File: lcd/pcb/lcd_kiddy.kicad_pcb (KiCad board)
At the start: 2 copper layers, 47 x 72 mm, 4 parts, among them J1 CONN_02X08, J3 BARREL_JACK, U1 ATMEGA168A-PU

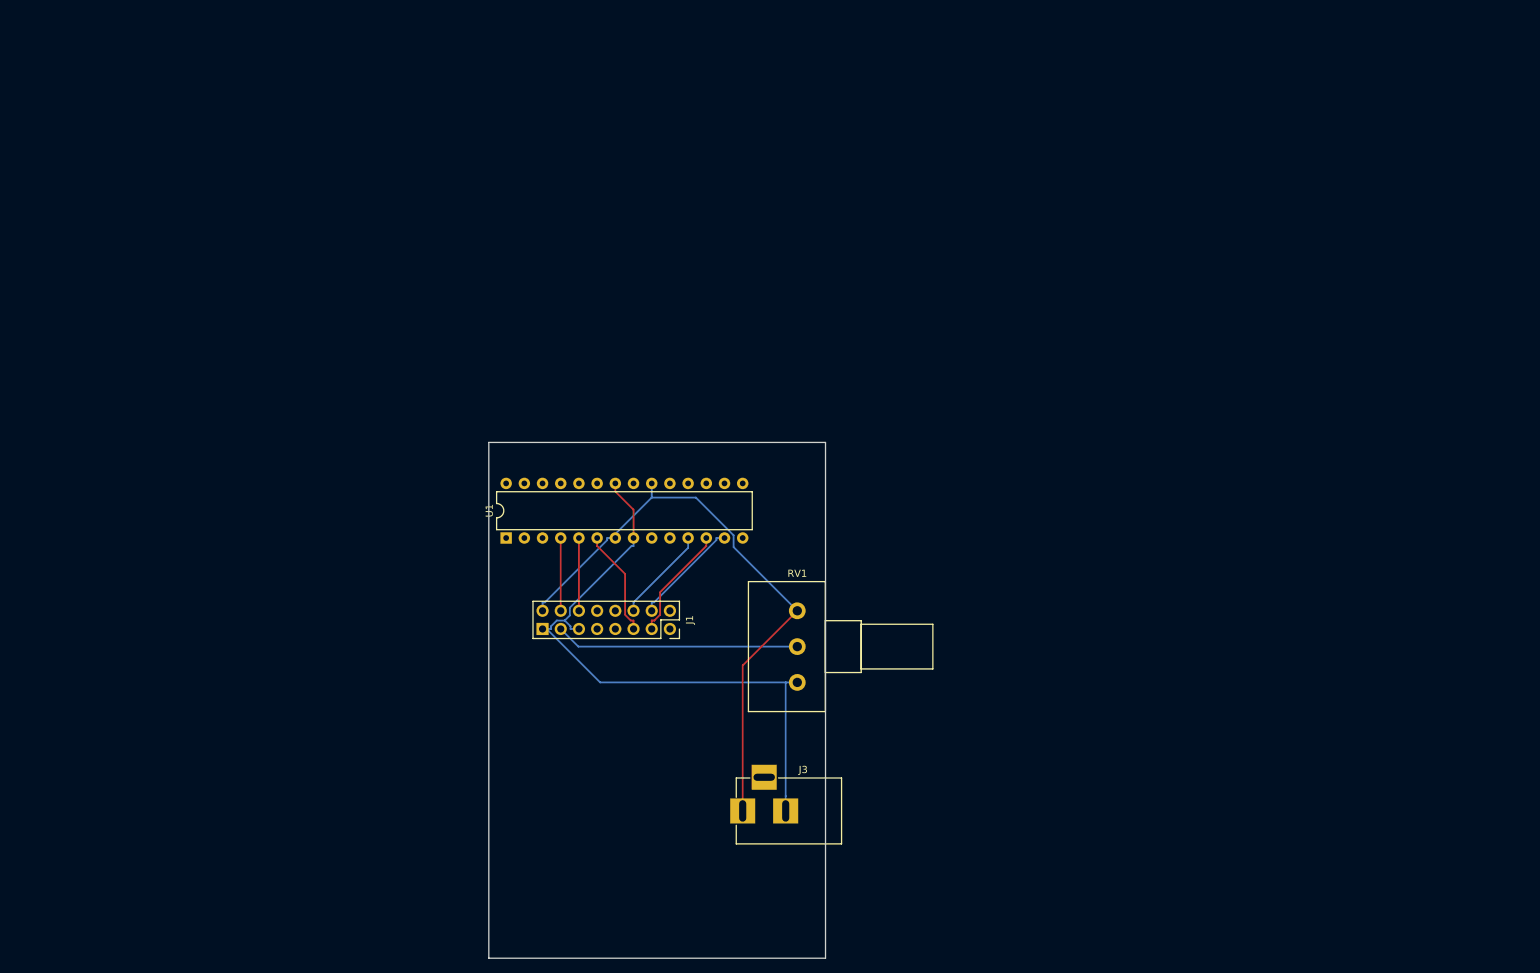
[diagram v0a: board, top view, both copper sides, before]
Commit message: LCDとatmega168aの配線方法を書いた。
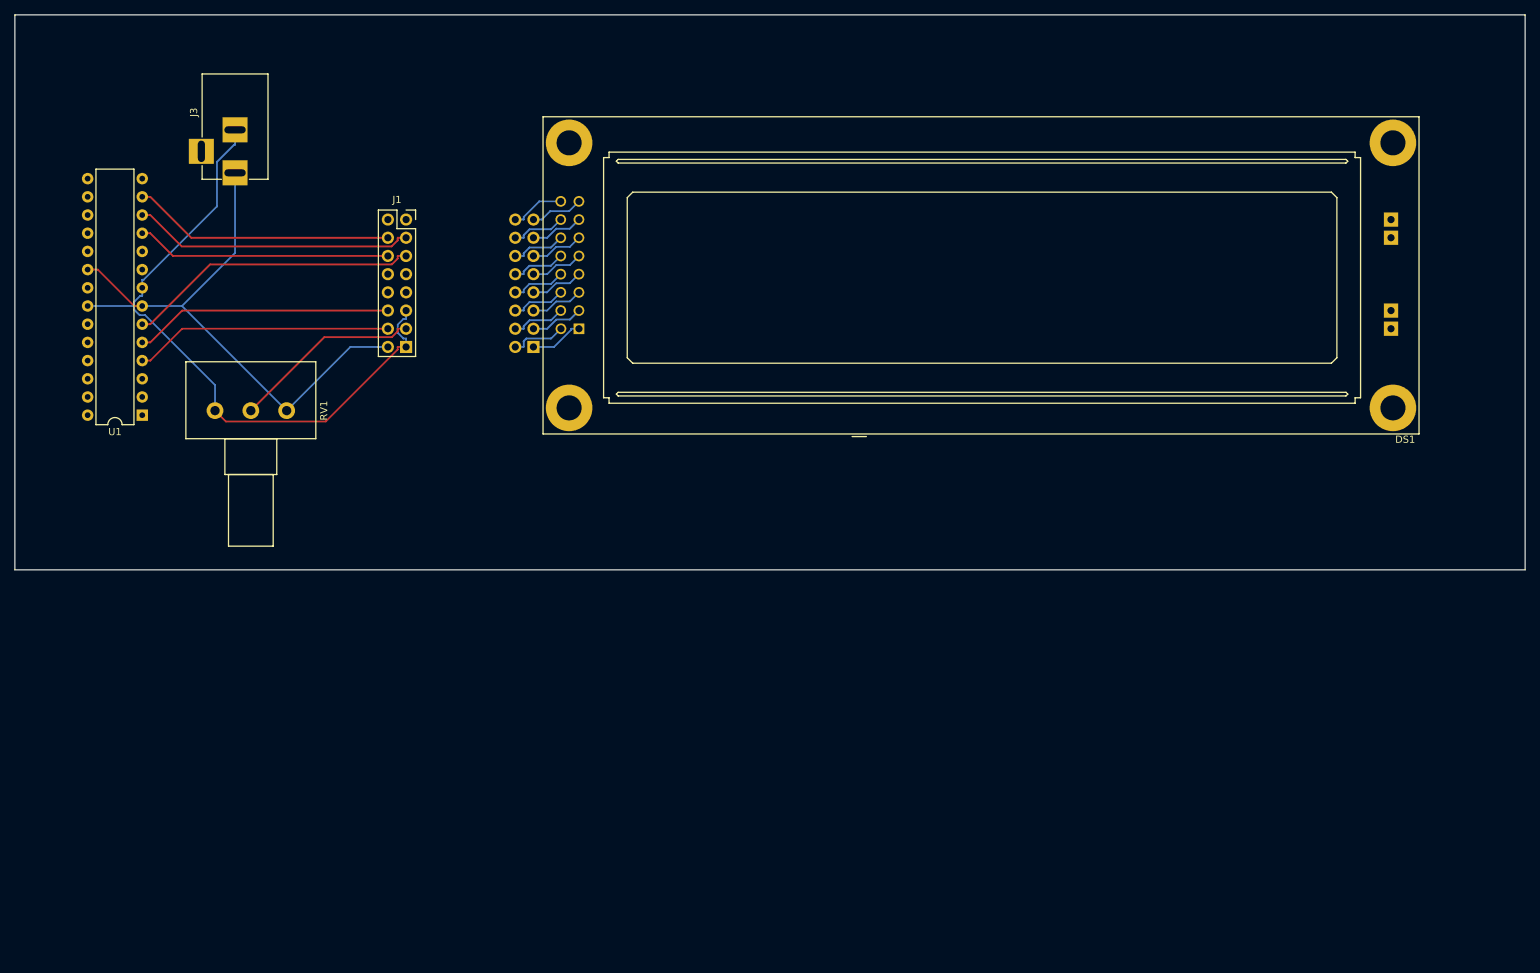
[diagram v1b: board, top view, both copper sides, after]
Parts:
- added DS1: LCD8X2, kiddy:LCD-2x8-AK, F.Cu at (177.8, 87.6)
- added J2: CONN_02X08, kiddy:PinHeader_2x08_P2.54mm_Vertical_R, B.Cu at (115.6, 97.8)
- moved J3 113.8 mm to (73.9, 73.5), turned to 270 degrees
- moved RV1 89.7 mm to (71.1, 106.7), turned to 270 degrees
- moved J1 68.0 mm to (97.8, 80.0), turned to 0 degrees
- moved U1 53.6 mm to (61.0, 107.3), turned to 180 degrees
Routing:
- net /PD4: track 15.0 -> 41.0 mm
- net /PD3: track 10.2 -> 36.1 mm
- net /PD2: track 10.2 -> 36.1 mm
- net /PD6: track 16.1 -> 39.4 mm
- net /PD5: track 13.3 -> 35.6 mm
- net /PD7: track 15.2 -> 36.7 mm
- net +5V: track 84.1 -> 75.4 mm
- net GND: track 86.8 -> 95.3 mm
- net /VDD: track 0.00 -> 7.90 mm
- net /RS: track 0.00 -> 7.62 mm
- net /D5: track 0.00 -> 7.62 mm
- net /D1: track 0.00 -> 7.62 mm
- net /D7: track 0.00 -> 7.62 mm
- net /E: track 0.00 -> 7.62 mm
- net /D3: track 0.00 -> 7.62 mm
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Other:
- board size 47 x 72 mm -> 210.8 x 77.5 mm

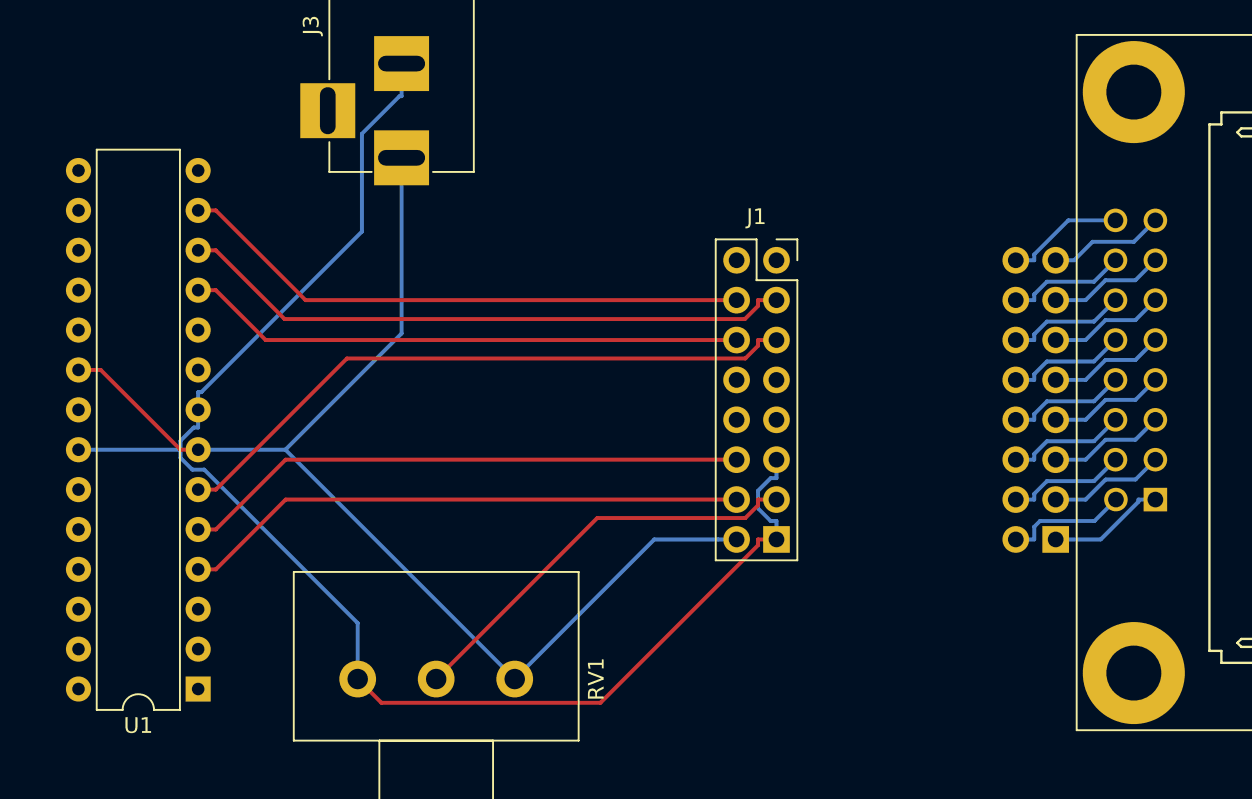
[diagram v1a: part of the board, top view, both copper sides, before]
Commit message: VEEとGNDを5kの可変抵抗で接続するようにした。
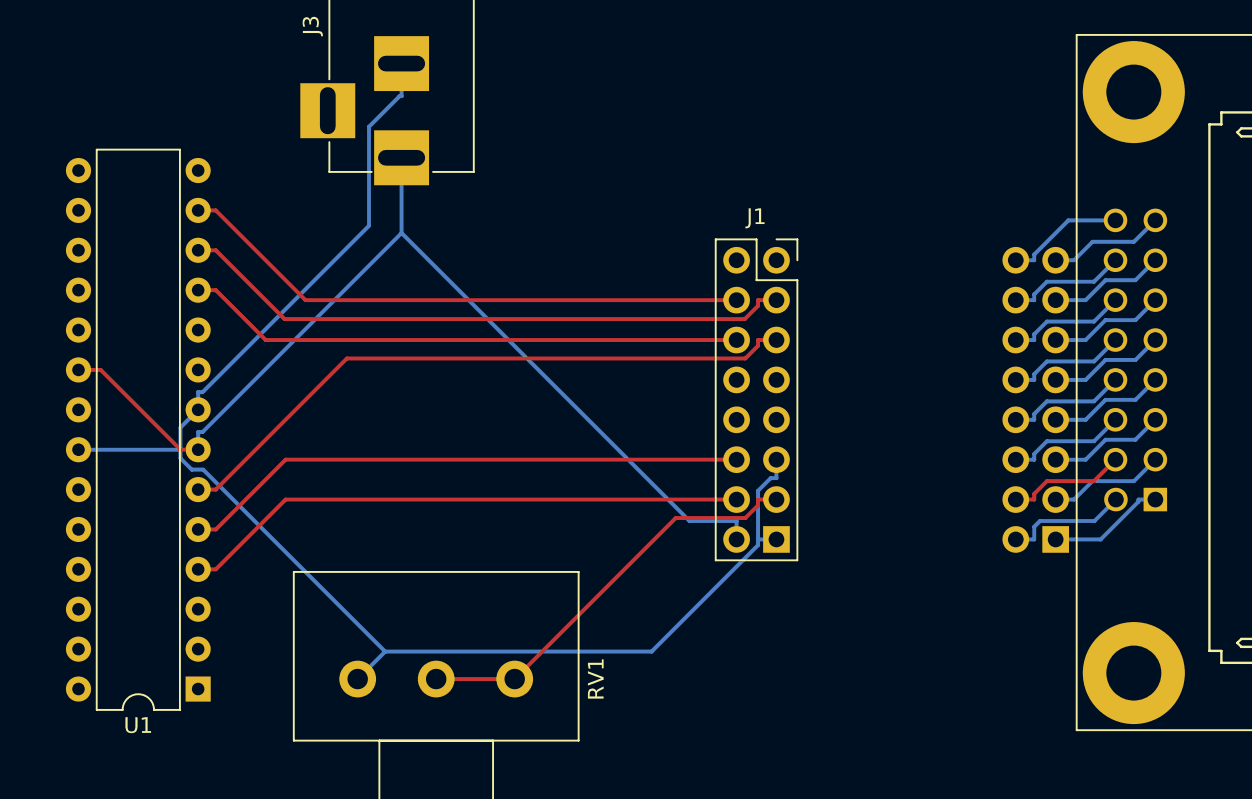
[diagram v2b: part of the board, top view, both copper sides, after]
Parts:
- U1: value ATMEGA168A-PU -> ATMEGA328-PU
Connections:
- RV1 pad 3: +5V -> Net-(J1-Pad3)
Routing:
- net +5V: track 75.4 -> 64.0 mm
- net GND: track 95.3 -> 92.2 mm
